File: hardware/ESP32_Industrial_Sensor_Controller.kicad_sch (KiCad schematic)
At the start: 15 parts, among them J1 Conn_01x06, SW1 Reset button, SW2 boot button, U1 AP2112K-3.3, U2 ESP32-WROOM-32, U3 SHT31-DIS

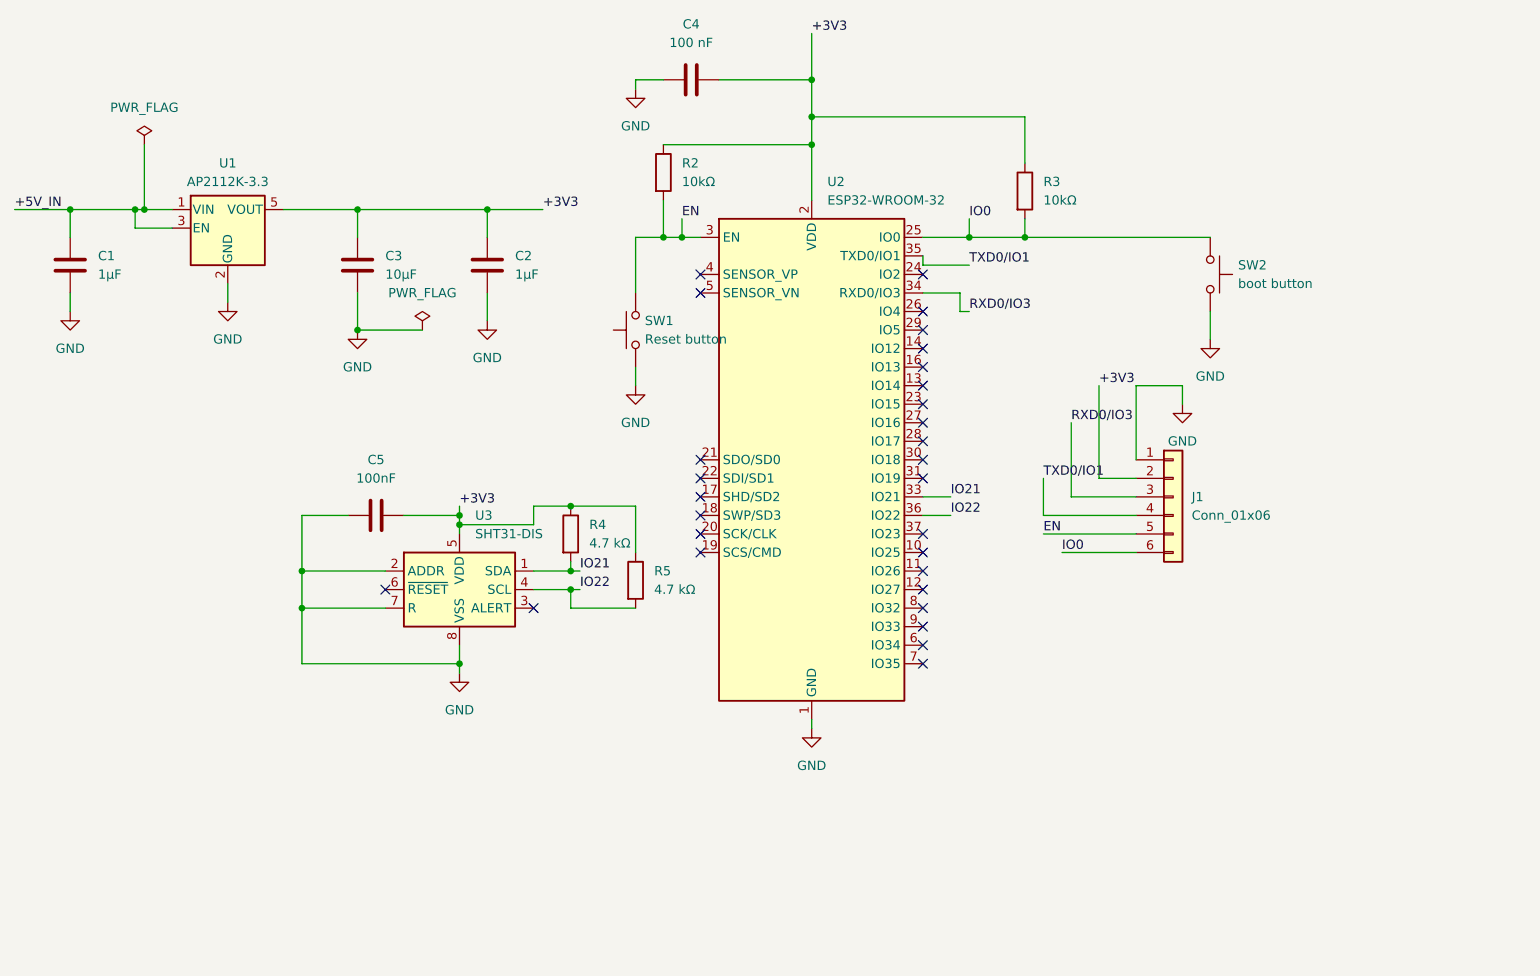
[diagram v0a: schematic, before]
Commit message: Populate title block details in schematic/PCB and update rendered assets
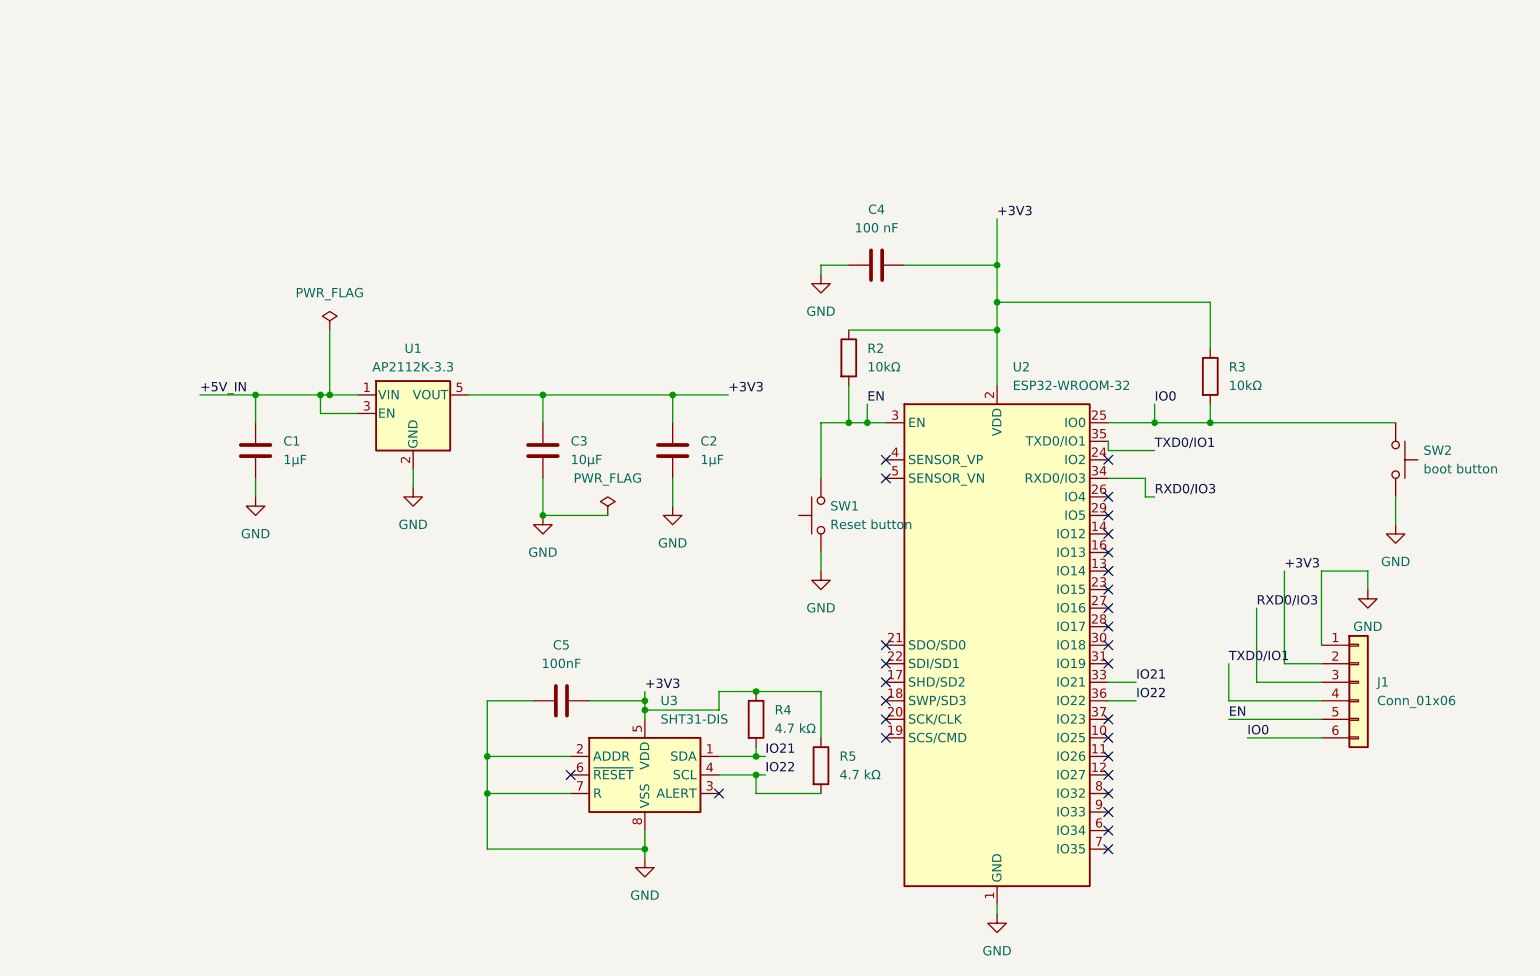
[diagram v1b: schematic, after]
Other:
- company: (none) -> Open Hardware Portfolio
- title: (none) -> ESP32 Industrial Sensor Controller
- moved on the sheet: C1, C2, C3, C4, C5, J1, R2, R3, R4, R5, SW1, SW2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
